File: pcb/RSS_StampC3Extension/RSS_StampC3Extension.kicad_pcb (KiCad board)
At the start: 2 copper layers, 81.8 x 72.1 mm, 32 parts, among them J1 5v_3Pi, J2 GND_3Pi, J5 I2C_3Pi, J6 3PI_SWTCH, J8 Conn_01x12_Pin, J9 Conn_01x10_Pin, Q1 2N7000, Q2 2N7000, Q3 BC337, Q4 TEPT4300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

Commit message: Fixed missing connections between phototransistors and GPIO0,1,4 in schematic. Also, GPIO 5 cannot be used for ADC when using Wifi. So moved previous connection from GPIO 5 to 4.  Added bigger text to pcb.  Updated test code to test functionality - all working.
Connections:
- Q4 pad 1: Net-(Q4-C) -> G0
- Q5 pad 1: Net-(Q5-C) -> G1
- Q6 pad 1: Net-(Q6-C) -> G4
- R10 pad 1: Net-(Q6-C) -> G4
- R8 pad 1: Net-(Q4-C) -> G0
- R9 pad 1: Net-(Q5-C) -> G1
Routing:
- net G4: track 10.8 -> 97.0 mm, vias 0 -> 1
- net G1: track 10.8 -> 81.2 mm, vias 0 -> 1
- net Net-(Q5-C): track 35.3 -> 0.00 mm
- net G0: track 10.8 -> 40.4 mm
- net Net-(Q6-C): track 25.1 -> 0.00 mm
- net Net-(Q4-C): track 23.1 -> 0.00 mm
- net Net-(J3-Pin_2): track 109.9 -> 128.4 mm
- net 3V3: track 119.9 -> 114.3 mm, vias 1 -> 0
- net G6: track 27.5 -> 31.7 mm, vias 0 -> 1
- net G8: track 50.4 -> 53.7 mm
- net SDA_5V: track 14.8 -> 12.1 mm
- net G5: track 14.1 -> 11.6 mm
- net G7: track 29.9 -> 32.2 mm, vias 1 -> 0
- net 5V: track 82.3 -> 83.6 mm
- net G9: track 52.0 -> 53.0 mm
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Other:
- board text added: "Robotics Science & Systems"
- board text added: "SEMTM0043 / SEMTM0042"
- board text added: "V2.0 Apr 2026"
- board text removed: "V1.0 Mar 2026"

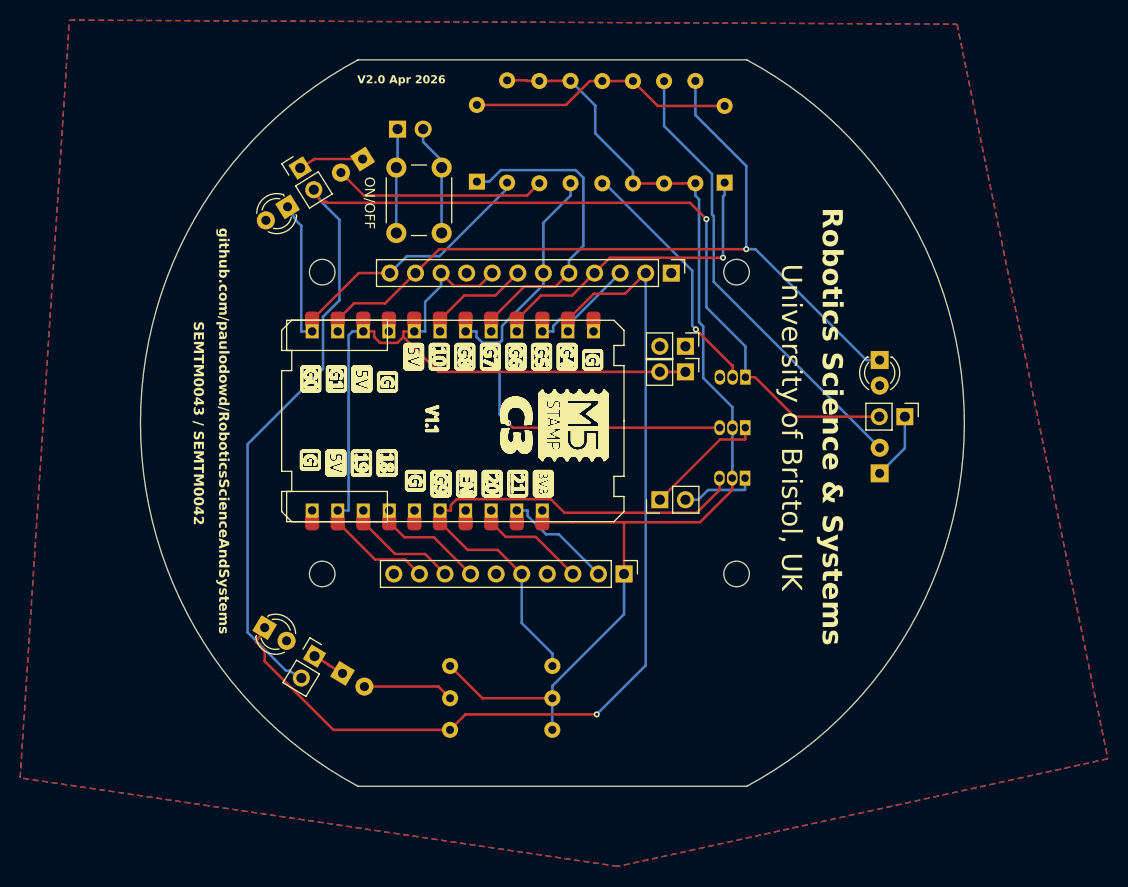
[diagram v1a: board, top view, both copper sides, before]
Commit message: Added a decoupling transistor, adjusted some text and added logo to silkscreen. Should be ready for production.
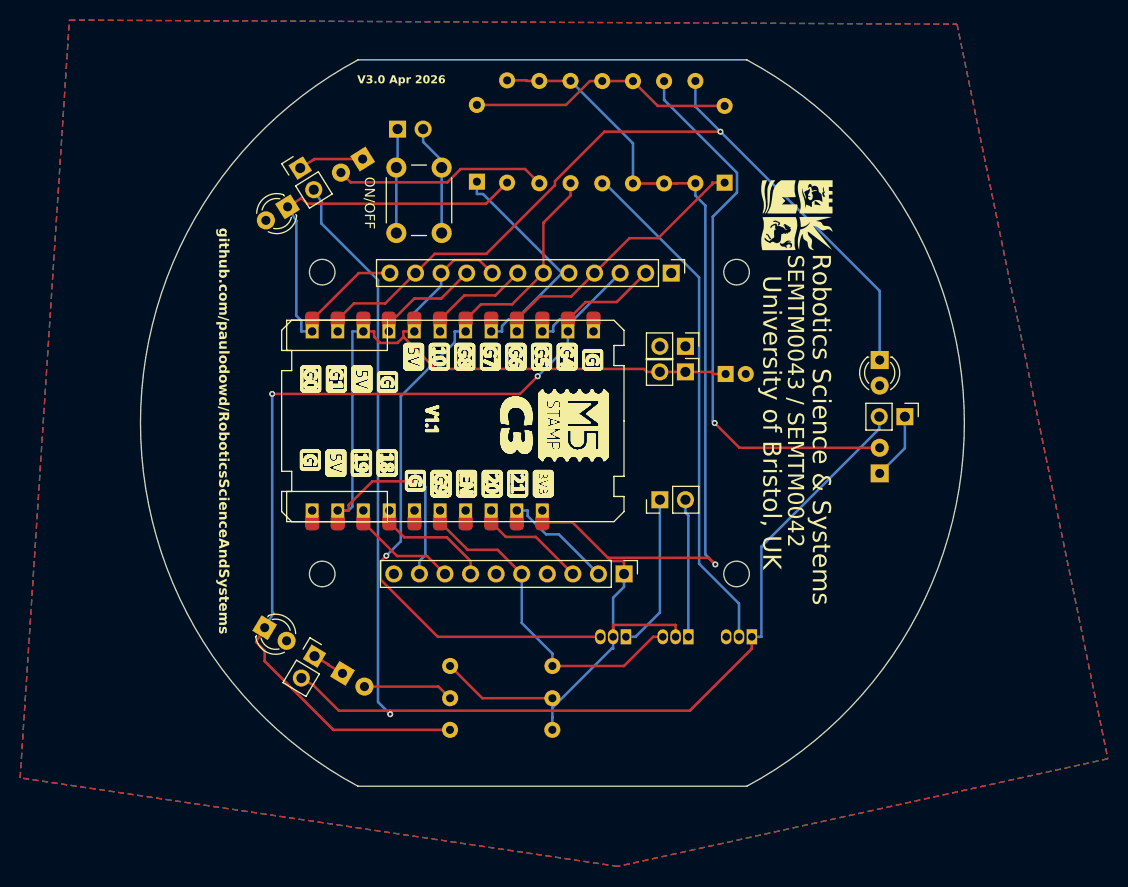
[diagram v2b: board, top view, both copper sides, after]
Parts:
- added C1: 1uf, PCM_Capacitor_THT_AKL:CP_Radial_D5.0mm_P2.00mm, B.Cu at (136.1, 89.4)
- added G***: LOGO, RSS_StampC3Extension:UoBLogo_8mm, F.Cu at (143.1, 73.6)
- moved Q3 25.8 mm to (138.7, 115.5)
- moved Q1 23.9 mm to (126.2, 115.5)
- moved Q2 16.7 mm to (132.4, 115.5)
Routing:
- net Net-(Q3-B): track 24.8 -> 50.8 mm, vias 1 -> 0
- net G8: track 53.7 -> 73.8 mm
- net G9: track 53.0 -> 34.0 mm
- net 5V: track 83.6 -> 96.4 mm, vias 0 -> 1
- net 3V3: track 114.3 -> 126.6 mm, vias 0 -> 1
- net GND: track 0.00 -> 10.6 mm
- net Net-(D3-A): track 45.3 -> 55.4 mm, vias 0 -> 1
- net G7: track 32.2 -> 24.6 mm
- net G0: track 40.4 -> 47.9 mm
- net SCL_5V: track 7.50 -> 13.7 mm
- net G4: track 97.0 -> 92.2 mm, vias 1 -> 2
- net Net-(J3-Pin_2): track 128.4 -> 132.9 mm
- net G6: track 31.7 -> 27.5 mm, vias 1 -> 0
- net SDA_5V: track 12.1 -> 15.6 mm
- net G1: track 81.2 -> 82.4 mm
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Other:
- board text added: "V3.0 Apr 2026"
- board text removed: "V2.0 Apr 2026"
